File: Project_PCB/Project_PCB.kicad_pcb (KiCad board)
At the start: 2 copper layers, 1 part, among them U1 ESP32-S3-WROOM-1

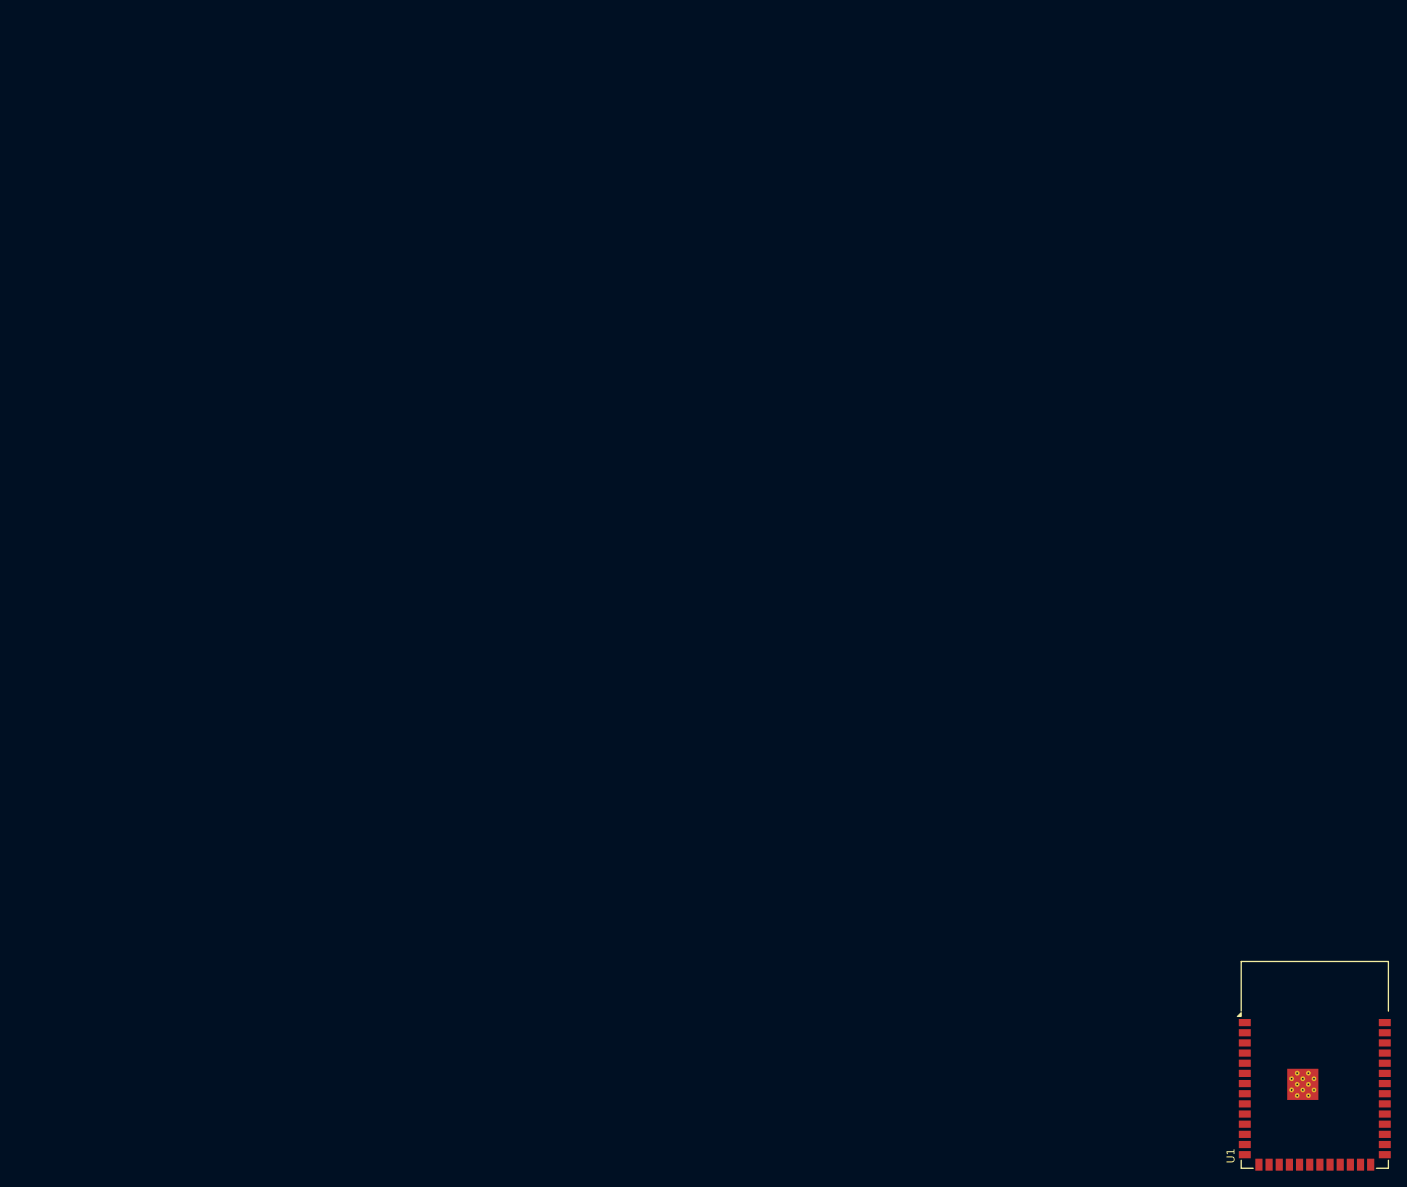
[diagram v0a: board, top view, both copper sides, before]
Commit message: Started work on PCB layout, made basic progress
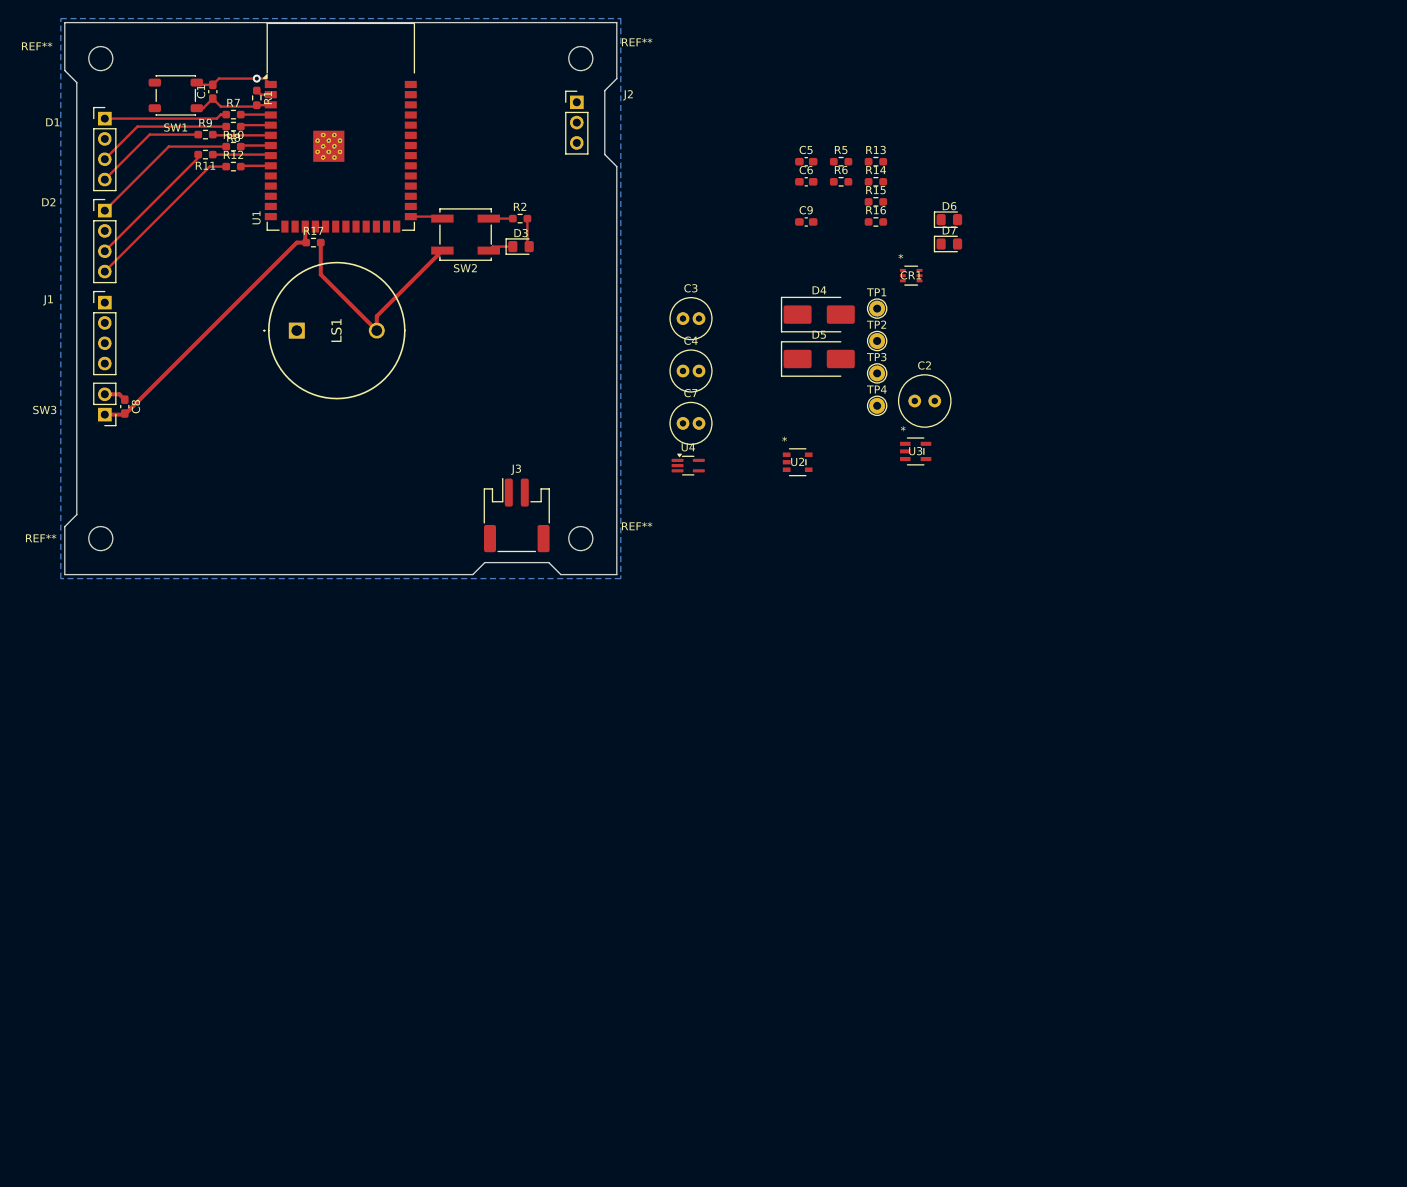
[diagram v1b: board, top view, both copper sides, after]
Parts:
- added C1: 1.0uF, Capacitor_SMD:C_0603_1608Metric_Pad1.08x0.95mm_HandSolder, F.Cu at (18.5, 8.64)
- added C2: 22uF, Capacitor_THT:C_Radial_D6.3mm_H7.0mm_P2.50mm, F.Cu at (106.2, 47.3)
- added C3: 4.7uF, Capacitor_THT:C_Radial_D5.0mm_H11.0mm_P2.00mm, F.Cu at (77.3, 37.0)
- added C4: 2.2uF, Capacitor_THT:C_Radial_D5.0mm_H11.0mm_P2.00mm, F.Cu at (77.3, 43.5)
- added C5: 0.1uF, Capacitor_SMD:C_0603_1608Metric_Pad1.08x0.95mm_HandSolder, F.Cu at (92.7, 17.4)
- added C6: 1.0uF, Capacitor_SMD:C_0603_1608Metric_Pad1.08x0.95mm_HandSolder, F.Cu at (92.7, 19.9)
- added C7: 10uF, Capacitor_THT:C_Radial_D5.0mm_H11.0mm_P2.00mm, F.Cu at (77.3, 50.1)
- added C8: 0.1uF, Capacitor_SMD:C_0603_1608Metric_Pad1.08x0.95mm_HandSolder, F.Cu at (7.50, 48.0)
- added C9: 0.1uF, Capacitor_SMD:C_0603_1608Metric_Pad1.08x0.95mm_HandSolder, F.Cu at (92.7, 24.9)
- added CR1: SMF05C.TCT, SMF05C:SC70-6L_SEM, F.Cu at (105.8, 31.6)
- added D1: LED_RKGB, Connector_PinHeader_2.54mm:PinHeader_1x04_P2.54mm_Vertical, F.Cu at (5.00, 12.0)
- added D2: LED_RKGB, Connector_PinHeader_2.54mm:PinHeader_1x04_P2.54mm_Vertical, F.Cu at (5.00, 23.5)
- added D3: Green, LED_SMD:LED_0805_2012Metric_Pad1.15x1.40mm_HandSolder, F.Cu at (57.0, 28.0)
- added D4: B2100, Diode_SMD:D_SMB_Handsoldering, F.Cu at (94.3, 36.5)
- added D5: B2100, Diode_SMD:D_SMB_Handsoldering, F.Cu at (94.3, 42.0)
- added D6: Red, LED_SMD:LED_0805_2012Metric_Pad1.15x1.40mm_HandSolder, F.Cu at (110.6, 24.6)
- added D7: Yellow, LED_SMD:LED_0805_2012Metric_Pad1.15x1.40mm_HandSolder, F.Cu at (110.6, 27.7)
- added J1: USB_C_2.0, Connector_PinHeader_2.54mm:PinHeader_1x04_P2.54mm_Vertical, F.Cu at (5.00, 35.0)
- added J2: Myoware Connector, Connector_PinHeader_2.54mm:PinHeader_1x03_P2.54mm_Vertical, F.Cu at (64.0, 9.96)
- added J3: Conn_01x02, Connector_JST:JST_PH_S2B-PH-SM4-TB_1x02-1MP_P2.00mm_Horizontal, F.Cu at (56.5, 61.6)
- added LS1: Speaker_Crystal, LD-BZPN-1705:LDBZPN1705, F.Cu at (29.0, 38.5)
- added R1: 10k, Resistor_SMD:R_0603_1608Metric_Pad0.98x0.95mm_HandSolder, F.Cu at (24.0, 9.41)
- added R10: 100, Resistor_SMD:R_0603_1608Metric_Pad0.98x0.95mm_HandSolder, F.Cu at (21.1, 15.5)
- added R11: 10, Resistor_SMD:R_0603_1608Metric_Pad0.98x0.95mm_HandSolder, F.Cu at (17.6, 16.5)
- added R12: 10, Resistor_SMD:R_0603_1608Metric_Pad0.98x0.95mm_HandSolder, F.Cu at (21.1, 18.0)
- added R13: 470, Resistor_SMD:R_0603_1608Metric_Pad0.98x0.95mm_HandSolder, F.Cu at (101.4, 17.4)
- added R14: 2.2k, Resistor_SMD:R_0603_1608Metric_Pad0.98x0.95mm_HandSolder, F.Cu at (101.4, 19.9)
- added R15: 36k, Resistor_SMD:R_0603_1608Metric_Pad0.98x0.95mm_HandSolder, F.Cu at (101.4, 22.4)
- added R16: 100k, Resistor_SMD:R_0603_1608Metric_Pad0.98x0.95mm_HandSolder, F.Cu at (101.4, 24.9)
- added R17: 10k, Resistor_SMD:R_0603_1608Metric_Pad0.98x0.95mm_HandSolder, F.Cu at (31.1, 27.5)
- added R2: 100, Resistor_SMD:R_0603_1608Metric_Pad0.98x0.95mm_HandSolder, F.Cu at (56.9, 24.5)
- added R5: 100k, Resistor_SMD:R_0603_1608Metric_Pad0.98x0.95mm_HandSolder, F.Cu at (97.0, 17.4)
- added R6: 1k, Resistor_SMD:R_0603_1608Metric_Pad0.98x0.95mm_HandSolder, F.Cu at (97.0, 19.9)
- added R7: 100, Resistor_SMD:R_0603_1608Metric_Pad0.98x0.95mm_HandSolder, F.Cu at (21.1, 11.5)
- added R8: 10, Resistor_SMD:R_0603_1608Metric_Pad0.98x0.95mm_HandSolder, F.Cu at (21.1, 13.0)
- added R9: 10, Resistor_SMD:R_0603_1608Metric_Pad0.98x0.95mm_HandSolder, F.Cu at (17.6, 14.0)
- added REF**: MountingHole_3mm, MountingHole:MountingHole_3mm, F.Cu at (4.50, 4.50)
- added REF**: MountingHole_3mm, MountingHole:MountingHole_3mm, F.Cu at (64.5, 64.5)
- added REF**: MountingHole_3mm, MountingHole:MountingHole_3mm, F.Cu at (4.50, 64.5)
- added REF**: MountingHole_3mm, MountingHole:MountingHole_3mm, F.Cu at (64.5, 4.50)
- added SW1: RESET, Button_Switch_SMD:SW_SPST_PTS647_Sx38, F.Cu at (13.9, 9.10)
- added SW2: BOOT, Button_Switch_SMD:SW_Push_1P1T_NO_CK_KSC6xxJ, F.Cu at (50.1, 26.5)
- added SW3: POWER, Connector_PinHeader_2.54mm:PinHeader_1x02_P2.54mm_Vertical, F.Cu at (5.00, 49.0)
- added TP1: 3V3_TEST, TestPoint:TestPoint_THTPad_D2.0mm_Drill1.0mm, F.Cu at (101.5, 35.8)
- added TP2: VBATT_TEST, TestPoint:TestPoint_THTPad_D2.0mm_Drill1.0mm, F.Cu at (101.5, 39.8)
- added TP3: GND_TEST, TestPoint:TestPoint_THTPad_D2.0mm_Drill1.0mm, F.Cu at (101.5, 43.9)
- added TP4: VUSB_TEST, TestPoint:TestPoint_THTPad_D2.0mm_Drill1.0mm, F.Cu at (101.5, 47.9)
- added U2: RT9080-33GJ5, RT9080:TSOT-23-5_RIT, F.Cu at (91.6, 55.0)
- added U3: MCP73831T-2ACI/OT, MCP73831:SOT-23-5_MC_MCH, F.Cu at (106.4, 53.6)
- added U4: LMV321, Package_TO_SOT_SMD:SOT-353_SC-70-5_Handsoldering, F.Cu at (77.9, 55.4)
- moved U1 169.0 mm to (34.5, 13.0)
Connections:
- U1 pad 10: unconnected-(U1-IO17-Pad10) -> Net-(U1-IO17)
- U1 pad 12: unconnected-(U1-IO8-Pad12) -> BATT/IO8
- U1 pad 17: unconnected-(U1-IO9-Pad17) -> POW/IO9
- U1 pad 4: unconnected-(U1-IO4-Pad4) -> D1R
- U1 pad 5: unconnected-(U1-IO5-Pad5) -> D1G
- U1 pad 6: unconnected-(U1-IO6-Pad6) -> D1B
- U1 pad 7: unconnected-(U1-IO7-Pad7) -> D2R
- U1 pad 8: unconnected-(U1-IO15-Pad8) -> D2G
- U1 pad 9: unconnected-(U1-IO16-Pad9) -> D2B
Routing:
- net GND: track 0.00 -> 40.5 mm, vias 0 -> 1
- net POW/IO9: track 0.00 -> 36.1 mm
- net Net-(D2-BA): track 0.00 -> 20.6 mm
- net Net-(D2-RA): track 0.00 -> 18.5 mm
- net Net-(D2-GA): track 0.00 -> 16.9 mm
- net Net-(D1-GA): track 0.00 -> 16.9 mm
- net Net-(D1-RA): track 0.00 -> 15.4 mm
- net Net-(D1-BA): track 0.00 -> 14.0 mm
- net ESP~{RST}: track 0.00 -> 10.3 mm
- net D2G: track 0.00 -> 7.30 mm
- net D1B: track 0.00 -> 7.29 mm
- net Net-(U1-IO0): track 0.00 -> 7.05 mm
- net +3V3: track 0.00 -> 4.74 mm
- net D1G: track 0.00 -> 3.82 mm
- net D2R: track 0.00 -> 3.81 mm
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- added copper zone on B.Cu, net GND
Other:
- board outline added: 69 x 69 mm

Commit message: Made progress on PCB layout; minor changes in schematic to ease routing
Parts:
- removed the C3 at (77.3, 37.0)
- added TP5: VIN, TestPoint:TestPoint_THTPad_D2.0mm_Drill1.0mm, F.Cu at (43.0, 55.0)
- moved D7 94.1 mm to (22.5, 61.0)
- moved CR1 94.1 mm to (12.0, 38.5), turned to 90 degrees
- moved TP4 92.9 mm to (9.00, 40.0)
- moved R13 91.0 mm to (22.6, 63.0)
- moved R14 86.9 mm to (27.4, 65.5)
- moved TP3 86.5 mm to (15.5, 52.4), turned to -90 degrees
- moved TP2 86.3 mm to (15.5, 46.4), turned to -90 degrees
- moved U3 80.1 mm to (26.7, 62.5), turned to 180 degrees
- moved R15 79.0 mm to (23.0, 32.4), turned to 90 degrees
- moved R16 78.5 mm to (23.0, 28.9), turned to 90 degrees
- moved C3 73.1 mm to (20.1, 34.0), turned to 180 degrees
- moved C6 71.2 mm to (22.5, 8.14), turned to 90 degrees
- moved D4 64.2 mm to (32.0, 52.0), turned to 180 degrees
- moved D5 64.1 mm to (32.0, 57.0), turned to 180 degrees
- moved U4 62.6 mm to (20.5, 30.3), turned to -90 degrees
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- renumbered C9 to C3
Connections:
- CR1 pad 1: unconnected-(CR1-Pad1) -> VBUS
- CR1 pad 4: VBUS -> unconnected-(CR1-Pad4)
- CR1 pad 5: ESP19/D- -> ESP20/D+
- CR1 pad 6: ESP20/D+ -> ESP19/D-
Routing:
- net GND: track 40.5 -> 99.5 mm
- net ESP19/D-: track 0.00 -> 31.9 mm, vias 0 -> 2
- net ESP20/D+: track 0.00 -> 28.4 mm
- net Net-(U1-IO17): track 0.00 -> 23.0 mm, vias 0 -> 1
- net Net-(J2-Pin_2): track 0.00 -> 22.2 mm
- net +BATT: track 0.00 -> 17.7 mm
- net VBUS: track 0.00 -> 10.0 mm, vias 0 -> 1
- net VIN: track 0.00 -> 9.71 mm
- net Net-(U1-IO0): track 7.05 -> 12.9 mm
- net Net-(U3-STAT): track 0.00 -> 5.10 mm
- net Net-(U4-+): track 0.00 -> 3.87 mm
- net POW/IO9: track 36.1 -> 39.3 mm
- net BATT/IO8: track 0.00 -> 2.66 mm
- net Net-(U3-PROG): track 0.00 -> 2.48 mm
- net Net-(D7-K): track 0.00 -> 2.07 mm
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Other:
- outline, holes or cut-outs redrawn

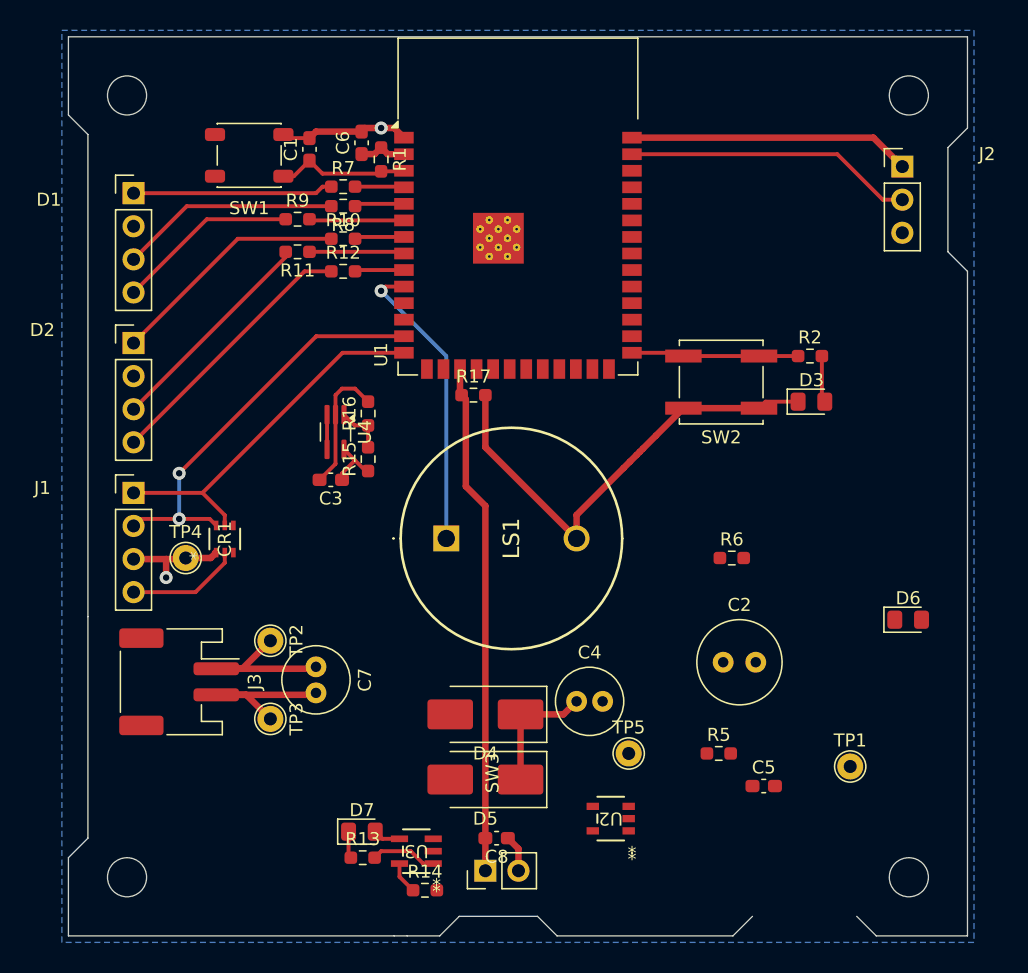
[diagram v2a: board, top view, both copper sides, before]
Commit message: Finished PCB design, added alignment tabs
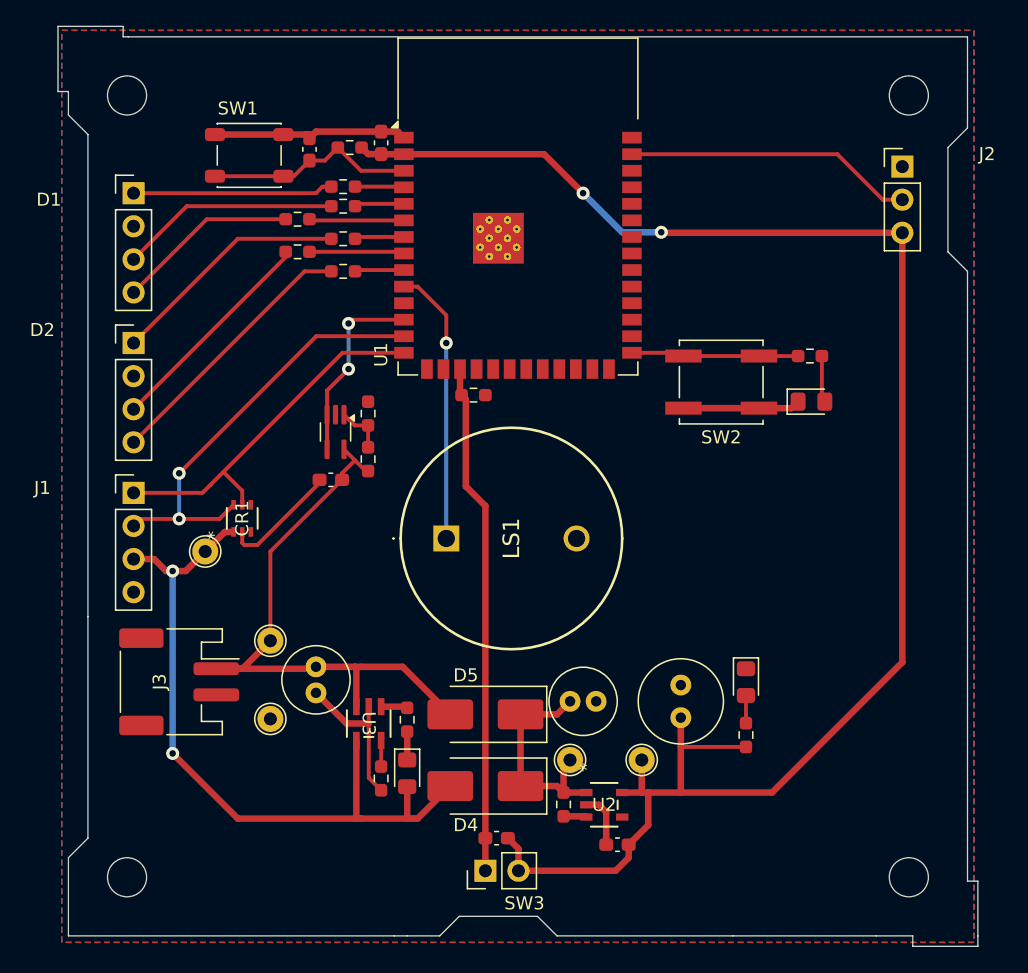
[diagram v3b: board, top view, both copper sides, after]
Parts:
- moved TP1 16.0 mm to (44.0, 55.5)
- moved R6 13.6 mm to (52.0, 53.6), turned to 90 degrees
- moved D6 13.3 mm to (52.0, 49.5), turned to -90 degrees
- moved R5 12.5 mm to (38.0, 58.9), turned to 90 degrees
- moved C5 12.1 mm to (42.1, 62.0), turned to 180 degrees
- moved R13 11.1 mm to (26.0, 52.4), turned to 90 degrees
- moved U3 10.5 mm to (23.0, 52.7), turned to -90 degrees
- moved R14 9.22 mm to (24.0, 56.9), turned to -90 degrees
- moved D7 5.67 mm to (26.0, 56.5), turned to -90 degrees
- moved D4 5.50 mm to (32.0, 57.5)
- moved C2 5.35 mm to (47.0, 52.2), turned to 90 degrees
- moved D5 5.00 mm to (32.0, 52.0)
- moved TP5 4.53 mm to (38.5, 55.5)
- moved R1 2.58 mm to (21.6, 8.50), turned to 180 degrees
- moved CR1 2.07 mm to (13.3, 37.0)
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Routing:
- net +3V3: track 6.51 -> 133.4 mm, vias 0 -> 2
- net GND: track 99.5 -> 49.2 mm, vias 1 -> 0
- net VBUS: track 10.0 -> 56.1 mm, vias 1 -> 2
- net +BATT: track 17.7 -> 46.7 mm
- net BATT/IO8: track 2.66 -> 14.7 mm, vias 0 -> 2
- net VIN: track 9.71 -> 17.7 mm
- net ESP~{RST}: track 10.3 -> 16.1 mm
- net Net-(U3-STAT): track 5.10 -> 2.04 mm
- net Net-(D6-A): track 0.00 -> 2.12 mm
- net Net-(U2-EN): track 0.00 -> 1.77 mm
- net Net-(U1-IO17): track 23.0 -> 21.3 mm
- net ESP19/D-: track 31.9 -> 33.5 mm
- added copper zone on F.Cu, net GND
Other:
- board size 69 x 69 mm -> 70.6 x 70.6 mm
